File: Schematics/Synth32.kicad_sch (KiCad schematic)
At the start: 1 part

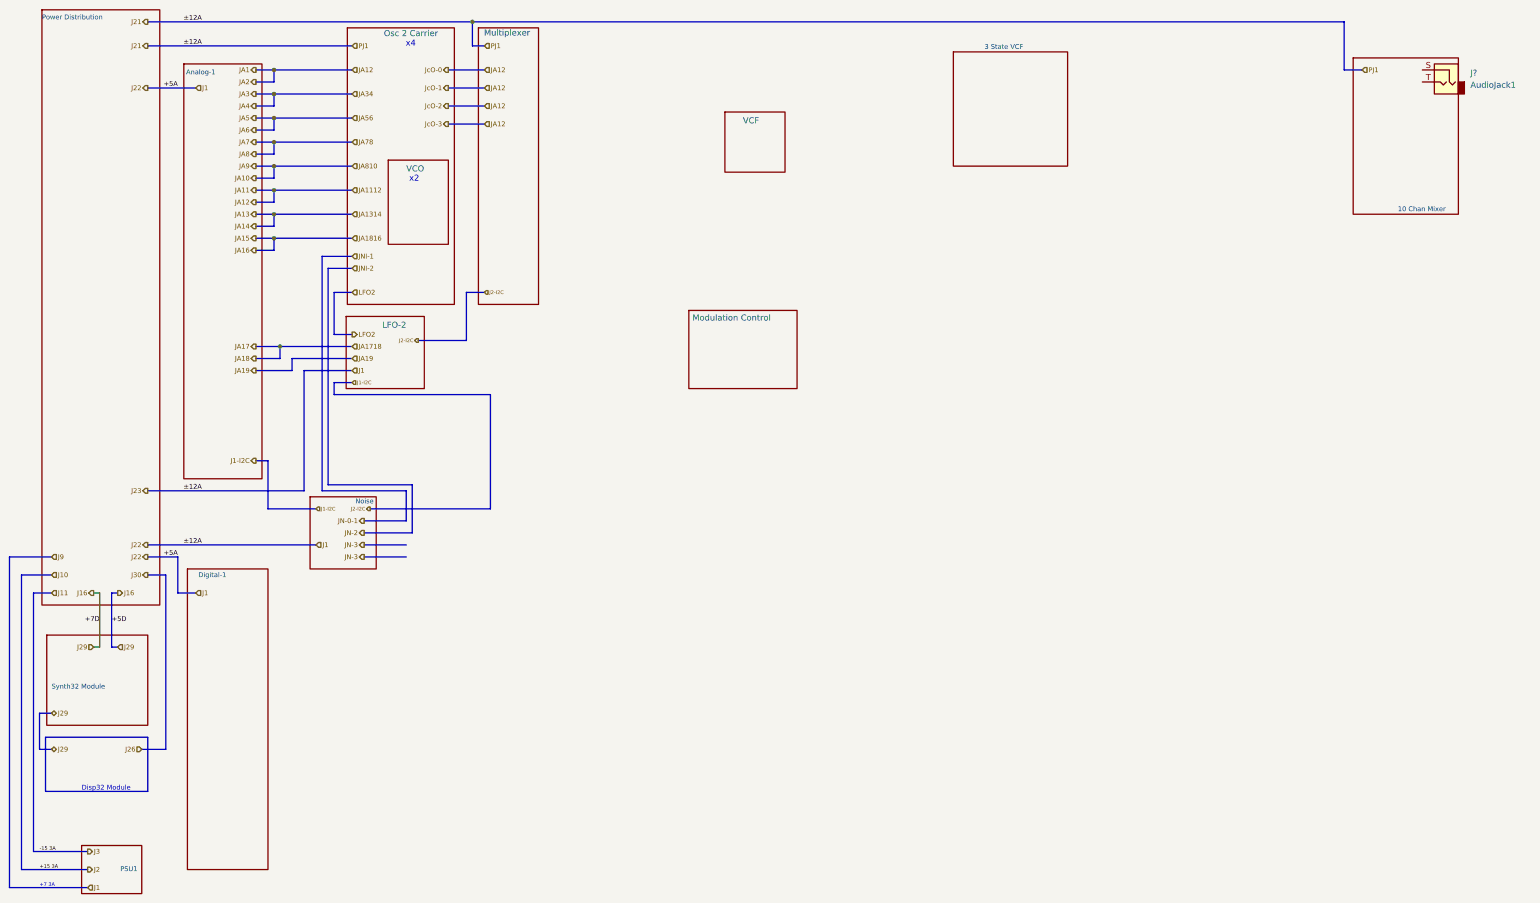
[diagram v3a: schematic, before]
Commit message: All Oscillators have thier own D/A converters and both LFOs are working.  Callibration functions.
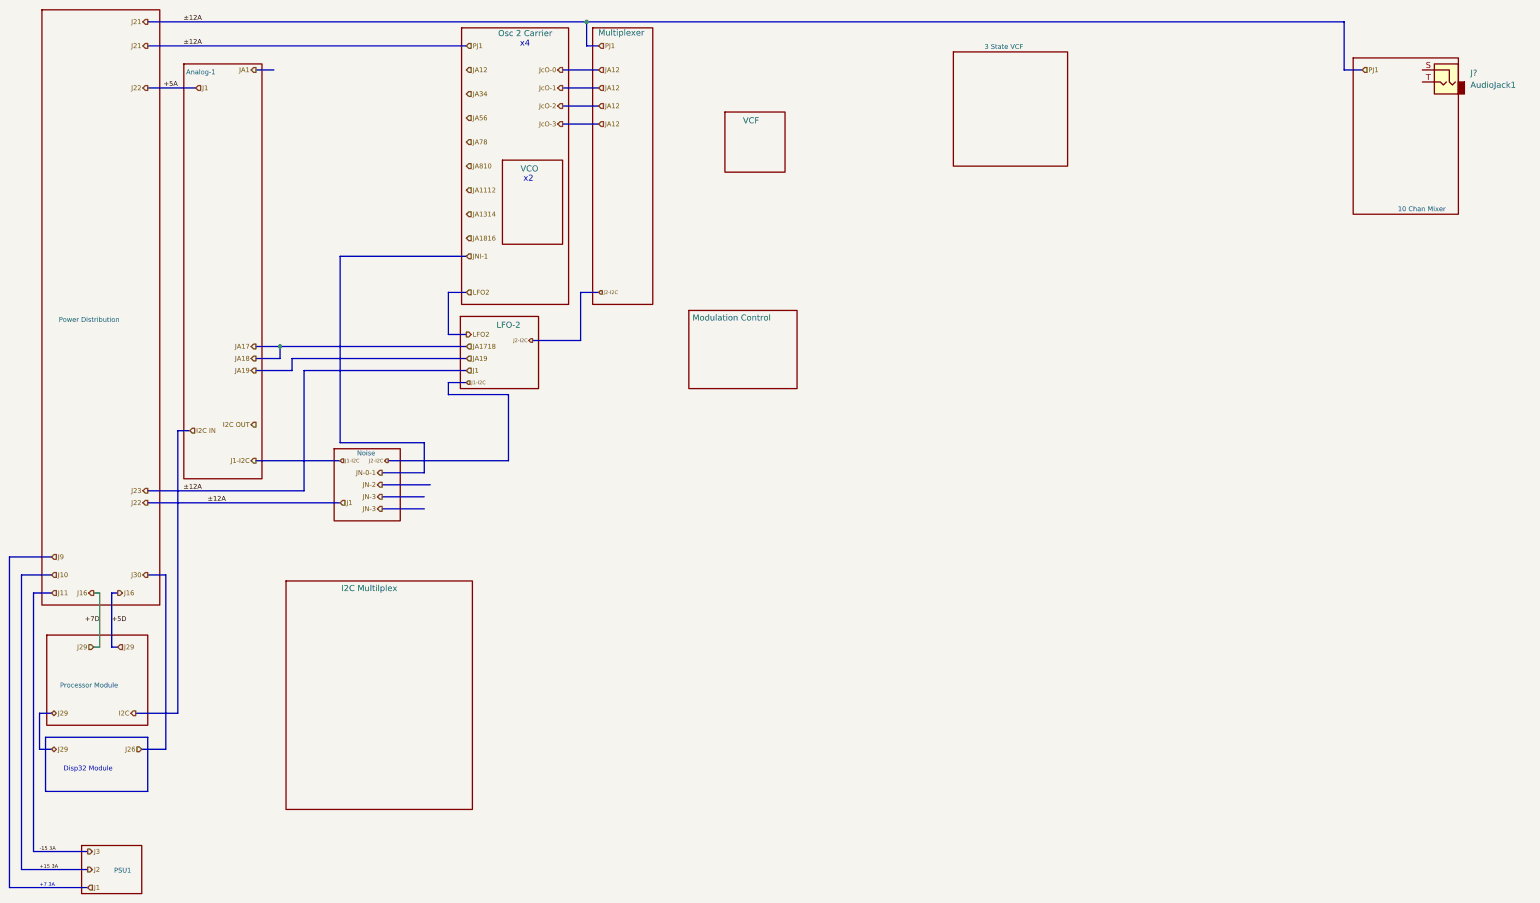
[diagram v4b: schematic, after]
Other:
- sheet Synth32 Module renamed Processor Module
- removed sheet Digital-1
- added sheet I2C Multilplex (I2C_Multiplax.kicad_sch)
- sheet Processor Module: file Digitial-1.kicad_sch -> Processor_Module.kicad_sch

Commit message: Fixed bugs in voice selection on configuration.  Reorganized schematics to have different master drawings for power and audio paths.  Started work on dual 3-pole state variable filter with resonance.
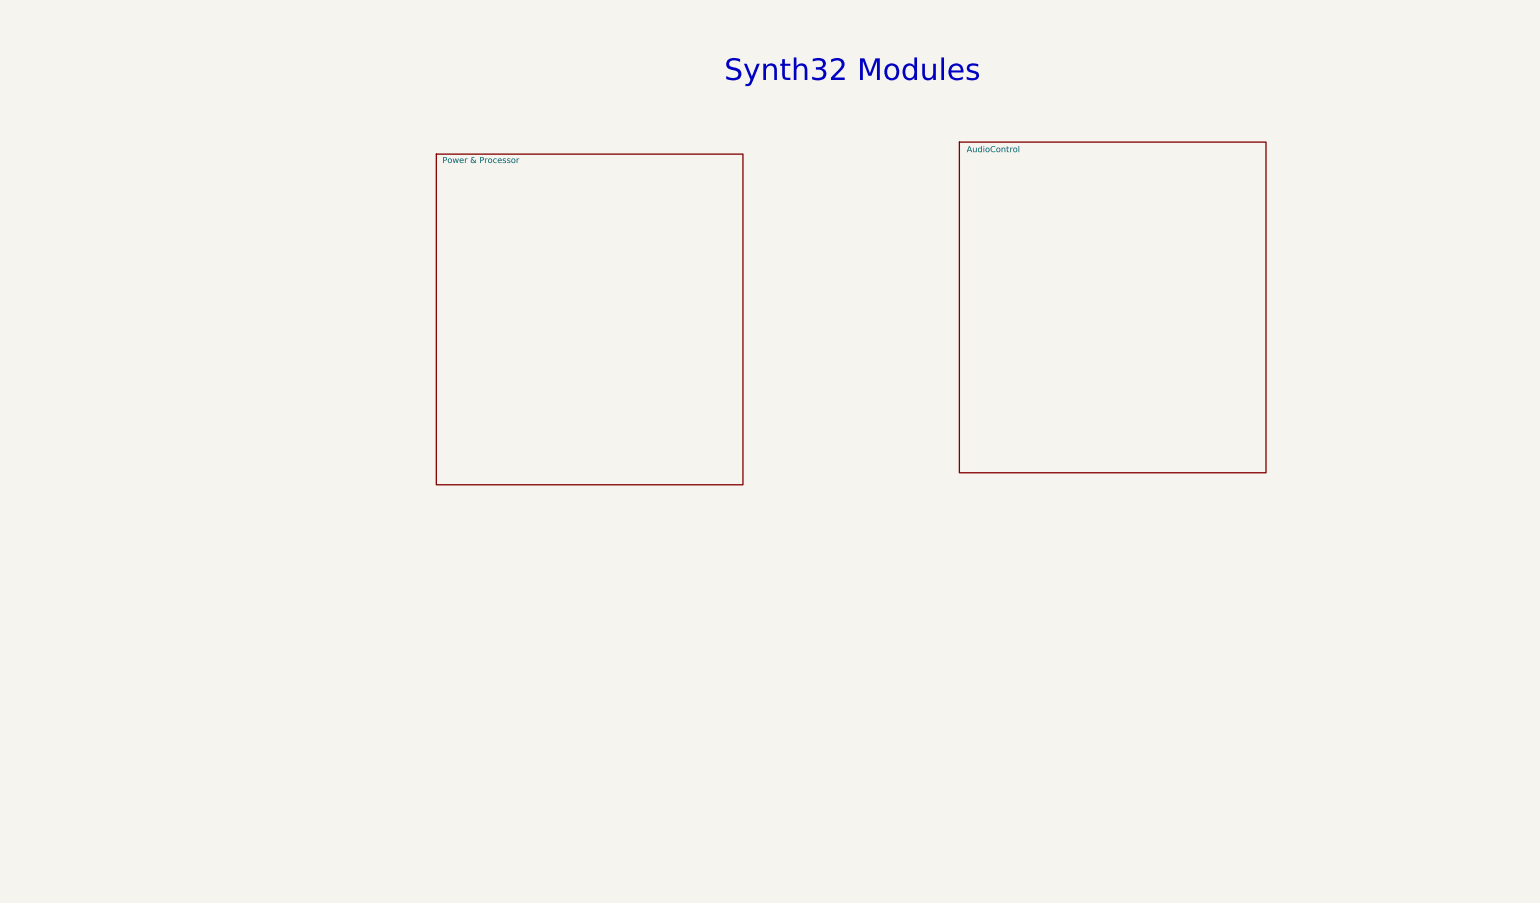
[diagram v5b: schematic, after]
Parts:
- removed J?: AudioJack1, symbol Connector:AudioJack2
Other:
- removed sheet 10 Chan Mixer
- removed sheet 3 State VCF
- removed sheet Analog-1
- removed sheet I2C Multilplex
- removed sheet LFO-2
- removed sheet Modulation Control
- removed sheet Multiplexer
- removed sheet Noise
- removed sheet Osc 2 Carrier
- removed sheet PSU1
- removed sheet Power Distribution
- removed sheet Processor Module
- removed sheet VCF
- removed sheet VCO
- added sheet AudioControl (AudioControl.kicad_sch)
- added sheet Power & Processor (PowerProcessor.kicad_sch)
- note added: "Synth32 Modules"
- note removed: "+7 3A"
- note removed: "Disp32 Module"
- note removed: "x2"
- note removed: "x4"

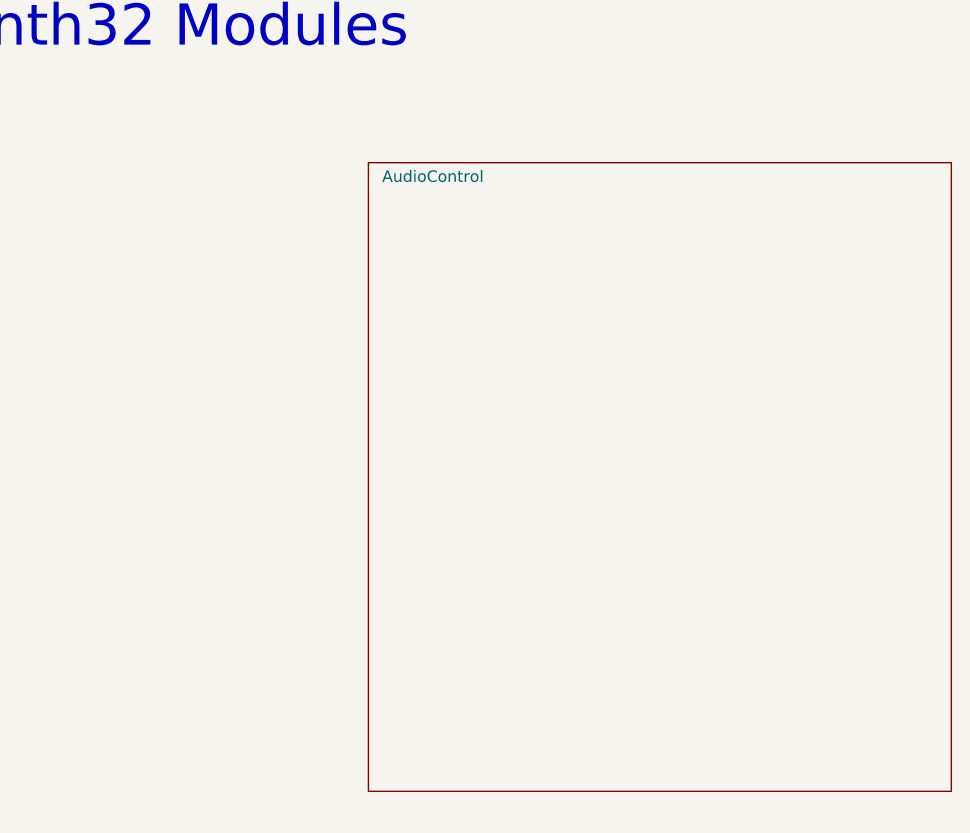
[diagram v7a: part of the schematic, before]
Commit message: Updated schematics, adding new low pass fillter and, added some statistical synth data to monitor.
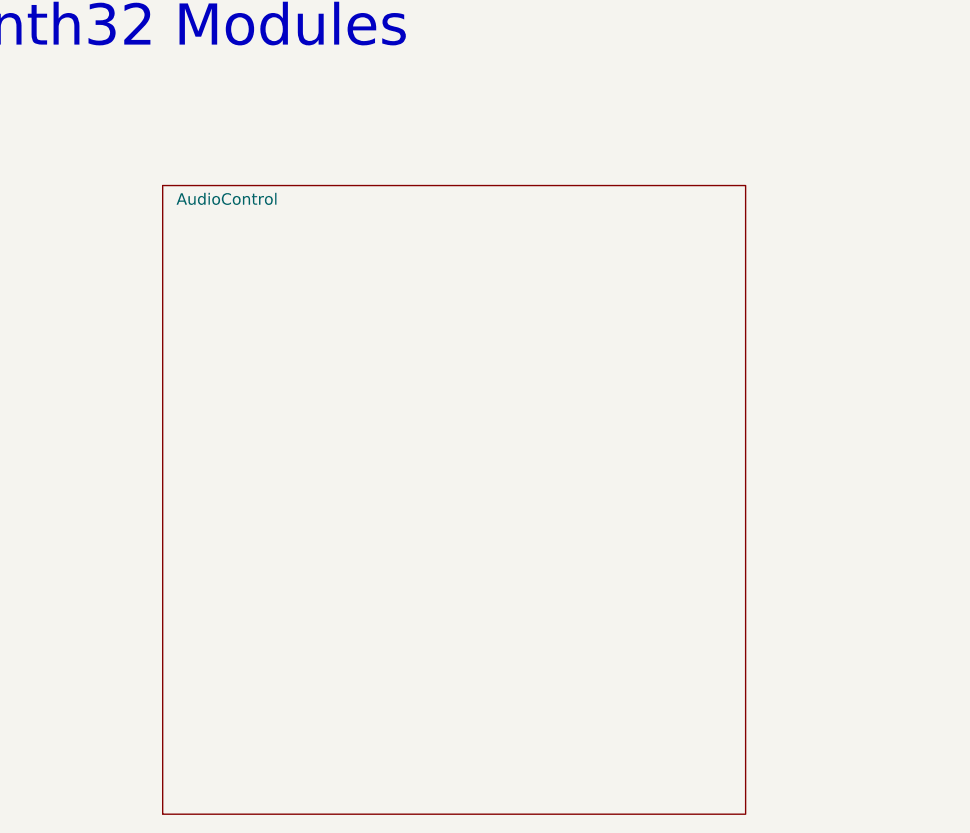
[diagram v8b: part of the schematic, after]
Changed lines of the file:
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@@
 	(title_block
 		(title "Top Interconnect")
-		(date "2025-11-28")
+		(date "2025-12-06")
 		(rev "3.2")
 		(comment 1 "In Development ")
@@
 	)
 	(sheet
-		(at 214.63 41.91)
+		(at 191.77 44.45)
 		(size 64.77 69.85)
 		(exclude_from_sim no)
@@
 		)
 		(property "Sheetname" "AudioControl"
-			(at 216.154 44.196 0)
+			(at 193.294 46.736 0)
 			(effects
 				(font
@@
 		)
 		(property "Sheetfile" "AudioControl.kicad_sch"
-			(at 214.63 81.8646 0)
+			(at 191.77 84.4046 0)
 			(effects
 				(font
